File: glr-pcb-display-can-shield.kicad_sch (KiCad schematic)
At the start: 17 parts, among them CN12 Conn_02x08_Odd_Even, CN5 Conn_01x10, CN6 Conn_01x08, CN7 Conn_01x08, CN8 Conn_01x06, IC1 AP64060WU-7, J1 Conn_02x02_Counter_Clockwise_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, J2 DB25_Socket

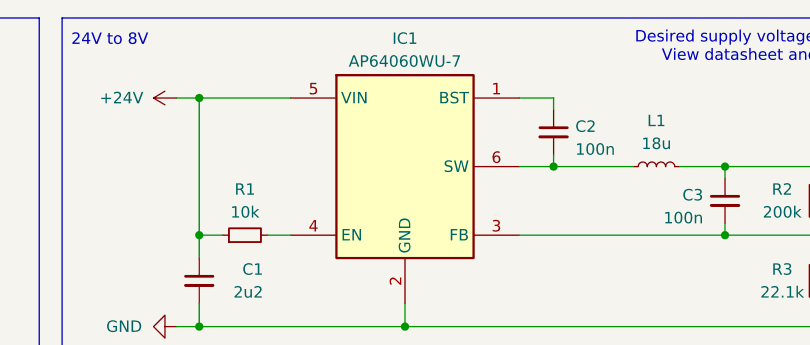
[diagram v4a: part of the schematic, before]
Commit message: add digikey/wuerth part numbers
* update README.md part list
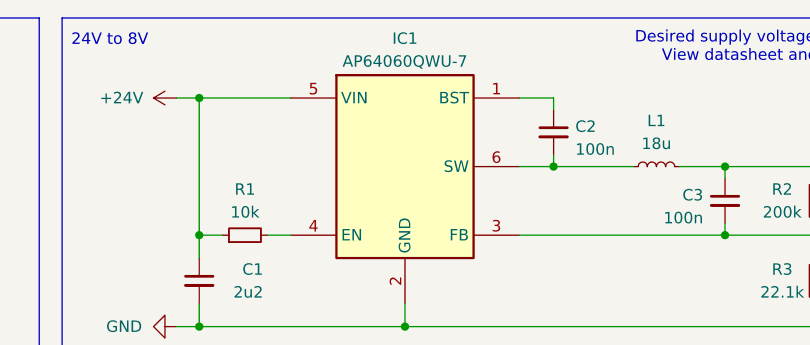
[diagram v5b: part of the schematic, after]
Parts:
- C1: DigiKey (none) -> 1276-1040-1-ND
- C2, C3, C6: DigiKey (none) -> 399-C0603C104K3RACTUCT-ND
- C4: DigiKey (none) -> 399-C0603C105K4RACTUCT-ND
- CN12: DigiKey (none) -> 732-5299-ND; WuerthElektronik (none) -> 61301621121
- CN5: DigiKey (none) -> 732-2670-ND; WuerthElektronik (none) -> 61301011121
- CN6, CN7: DigiKey (none) -> 732-5321-ND; WuerthElektronik (none) -> 61300811121
- CN8: DigiKey (none) -> 732-5319-ND; WuerthElektronik (none) -> 61300611121
- IC1: value AP64060WU-7 -> AP64060QWU-7; DigiKey (none) -> 31-AP64060QWU-7CT-ND
- J1: DigiKey (none) -> 732-643250100304-ND; WuerthElektronik (none) -> 643250100304
- J2: DigiKey (none) -> 732-61802525023-ND; WuerthElektronik (none) -> 61802525023
- L1: DigiKey (none) -> 732-74479889310CT-ND; WuerthElektronik (none) -> 74479889310
- R1: DigiKey (none) -> 311-10.0KHRCT-ND
- R2: DigiKey (none) -> P200KDBCT-ND
- R3: DigiKey (none) -> 311-22.1KHRCT-ND
